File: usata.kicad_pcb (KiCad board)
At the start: 2 copper layers, 20 x 50 mm, 2 parts, among them J1 FH28K-28S-0.5SH, J2 2023246-2

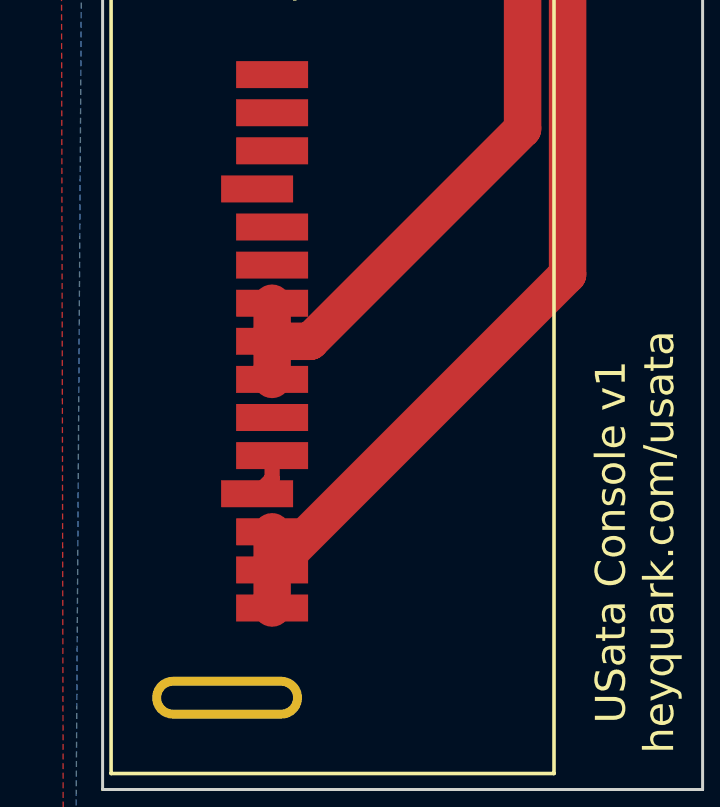
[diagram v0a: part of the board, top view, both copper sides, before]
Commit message: Minor fixes
This fixes the pad connections between P6 and P7, P9 and P10, P12 and P13 and the end of P15. Also it removes some redundant lines and adds a new connection between P4 and P5. Note that I have no idea how to fix the GND fill below P15 through.

Signed-off-by: Thomas Rohloff <v10lator@myway.de>
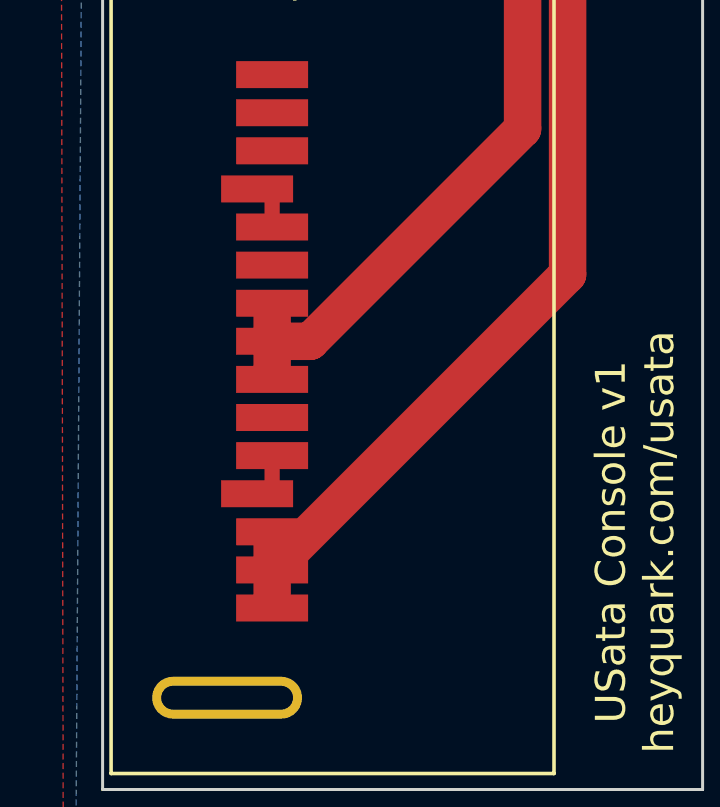
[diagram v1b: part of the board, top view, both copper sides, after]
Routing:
- net +12V: track 47.0 -> 46.2 mm
- net GND: track 11.9 -> 12.6 mm
- net +5V: track 35.4 -> 34.9 mm
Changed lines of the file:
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@@
     (effects (font (size 1 1) (thickness 0.15)))
   )
+  (segment (start 45.65 69.937025) (end 45.65 71.007037) (width 0.508) (layer "F.Cu") (net 6))
   (segment (start 49.25 56) (end 52 56) (width 0.1524) (layer "F.Cu") (net 6))
   (segment (start 51 54.5) (end 50.75 54.25) (width 0.1524) (layer "F.Cu") (net 6))
   (segment (start 52 51.5) (end 50.5 51.5) (width 0.25) (layer "F.Cu") (net 6))
-  (segment (start 45.65 78.869988) (end 45.65 79.639988) (width 0.508) (layer "F.Cu") (net 6))
+  (segment (start 45.65 78.869988) (end 45.65 79.94) (width 0.508) (layer "F.Cu") (net 6))
   (segment (start 52 46.25) (end 50.75 46.25) (width 0.75) (layer "F.Cu") (net 6))
   (segment (start 52 54.5) (end 51 54.5) (width 0.1524) (layer "F.Cu") (net 6))
   (segment (start 52 58.5) (end 52 57.5) (width 0.1524) (layer "F.Cu") (net 6))
   (segment (start 52 57.5) (end 51 57.5) (width 0.1524) (layer "F.Cu") (net 6))
-  (segment (start 45.65 79.639988) (end 45.15 80.139988) (width 0.508) (layer "F.Cu") (net 6))
   (segment (start 52 49.75) (end 50.75 49.75) (width 0.75) (layer "F.Cu") (net 6))
   (segment (start 51 57.5) (end 50.75 57.75) (width 0.1524) (layer "F.Cu") (net 6))
@@
   (segment (start 52 48) (end 53.3548 48) (width 1.25) (layer "F.Cu") (net 10))
   (segment (start 54 48.6452) (end 54 67.979988) (width 1.25) (layer "F.Cu") (net 10))
-  (segment (start 45.65 75.059988) (end 45.65 76.329988) (width 1.25) (layer "F.Cu") (net 10))
-  (segment (start 45.65 73.789988) (end 45.65 75.059988) (width 1.25) (layer "F.Cu") (net 10))
+  (segment (start 45.65 74) (end 45.65 76) (width 1.25) (layer "F.Cu") (net 10))
   (segment (start 53.3548 48) (end 54 48.6452) (width 1.25) (layer "F.Cu") (net 10))
   (segment (start 55.5 72.829988) (end 45.65 82.679988) (width 1.25) (layer "F.Cu") (net 13))
   (segment (start 52 44.5) (end 53.3548 44.5) (width 1.25) (layer "F.Cu") (net 13))
   (segment (start 55.5 46.6452) (end 55.5 72.829988) (width 1.25) (layer "F.Cu") (net 13))
-  (segment (start 45.65 82.679988) (end 45.65 81.409988) (width 1.25) (layer "F.Cu") (net 13))
-  (segment (start 45.65 82.679988) (end 45.65 83.949988) (width 1.25) (layer "F.Cu") (net 13))
+  (segment (start 45.65 83.5) (end 45.65 81.8) (width 1.25) (layer "F.Cu") (net 13))
   (segment (start 53.3548 44.5) (end 55.5 46.6452) (width 1.25) (layer "F.Cu") (net 13))
   (segment (start 47.450001 53.46) (end 47.932601 53.9426) (width 0.1524) (layer "F.Cu") (net 14))
